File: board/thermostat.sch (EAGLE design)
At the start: 14 parts, among them IC1 7805TV, Q1 PSMN4R3-30PL

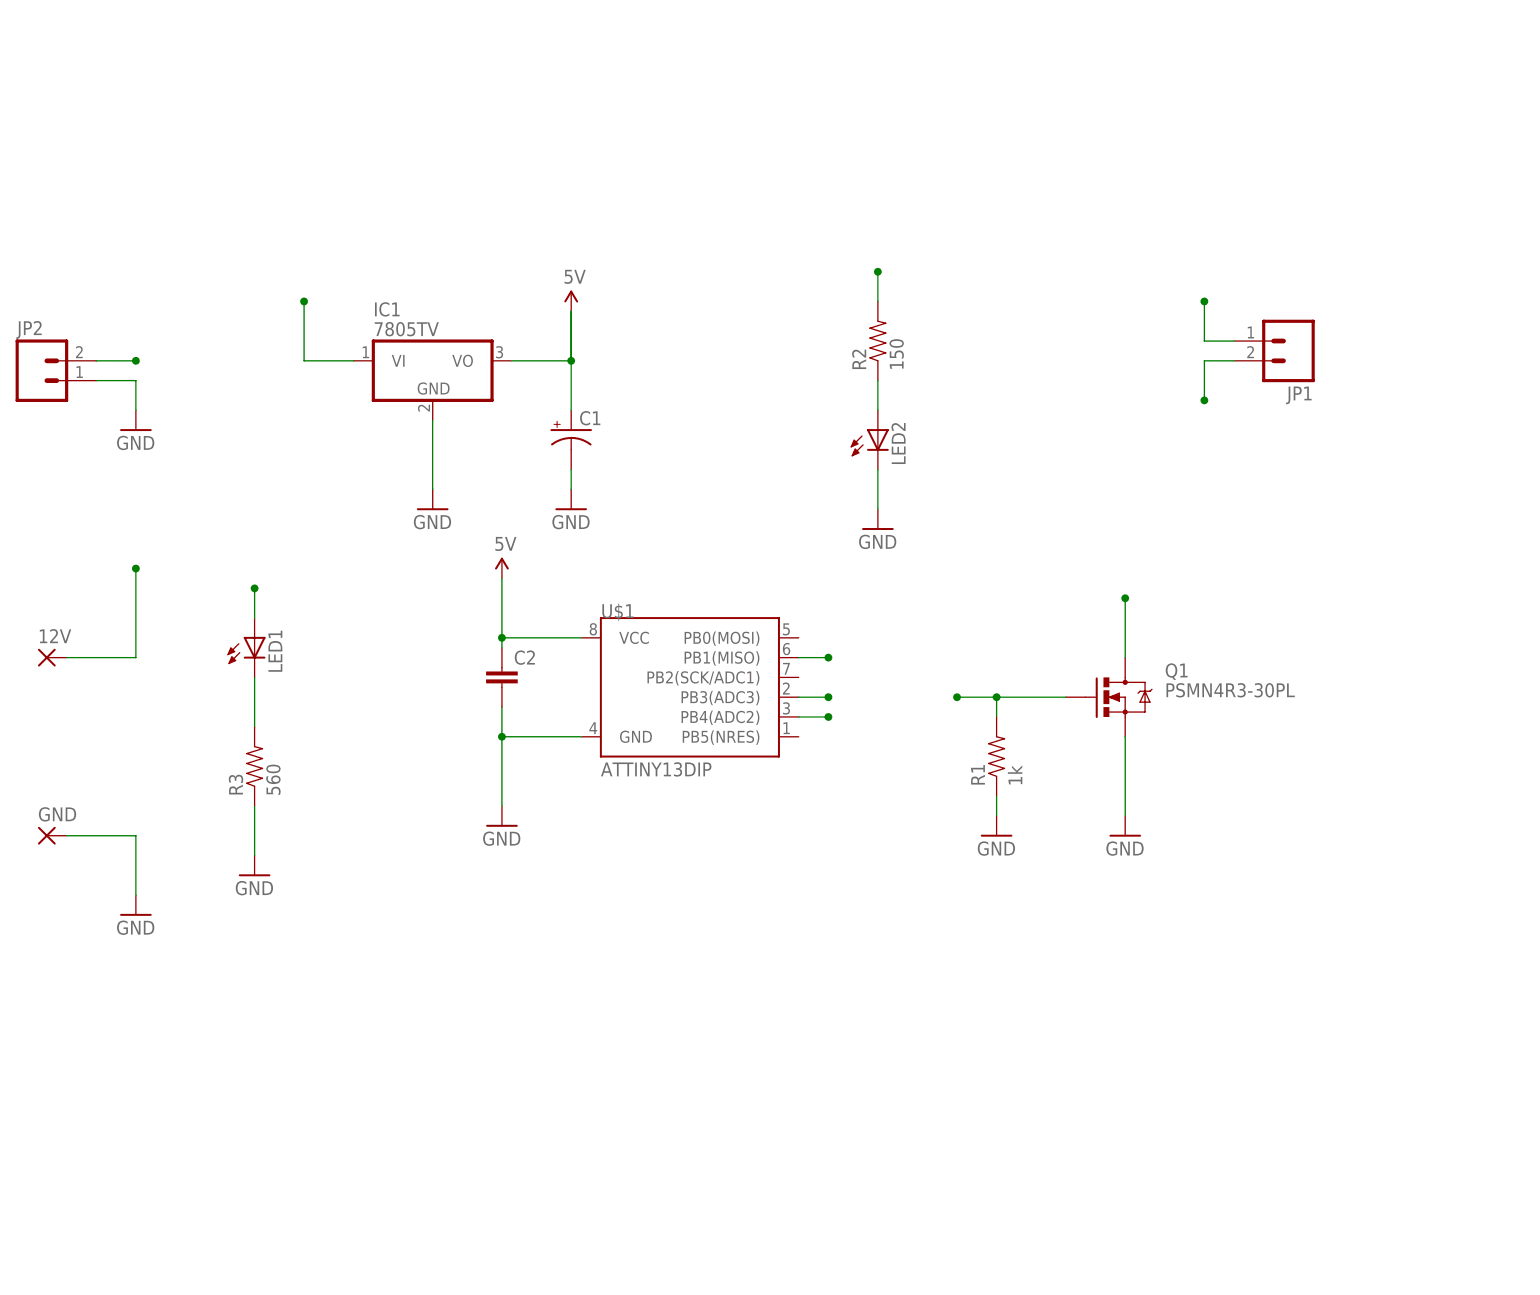
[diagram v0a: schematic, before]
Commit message: WIP: Protecting input and creating schematic
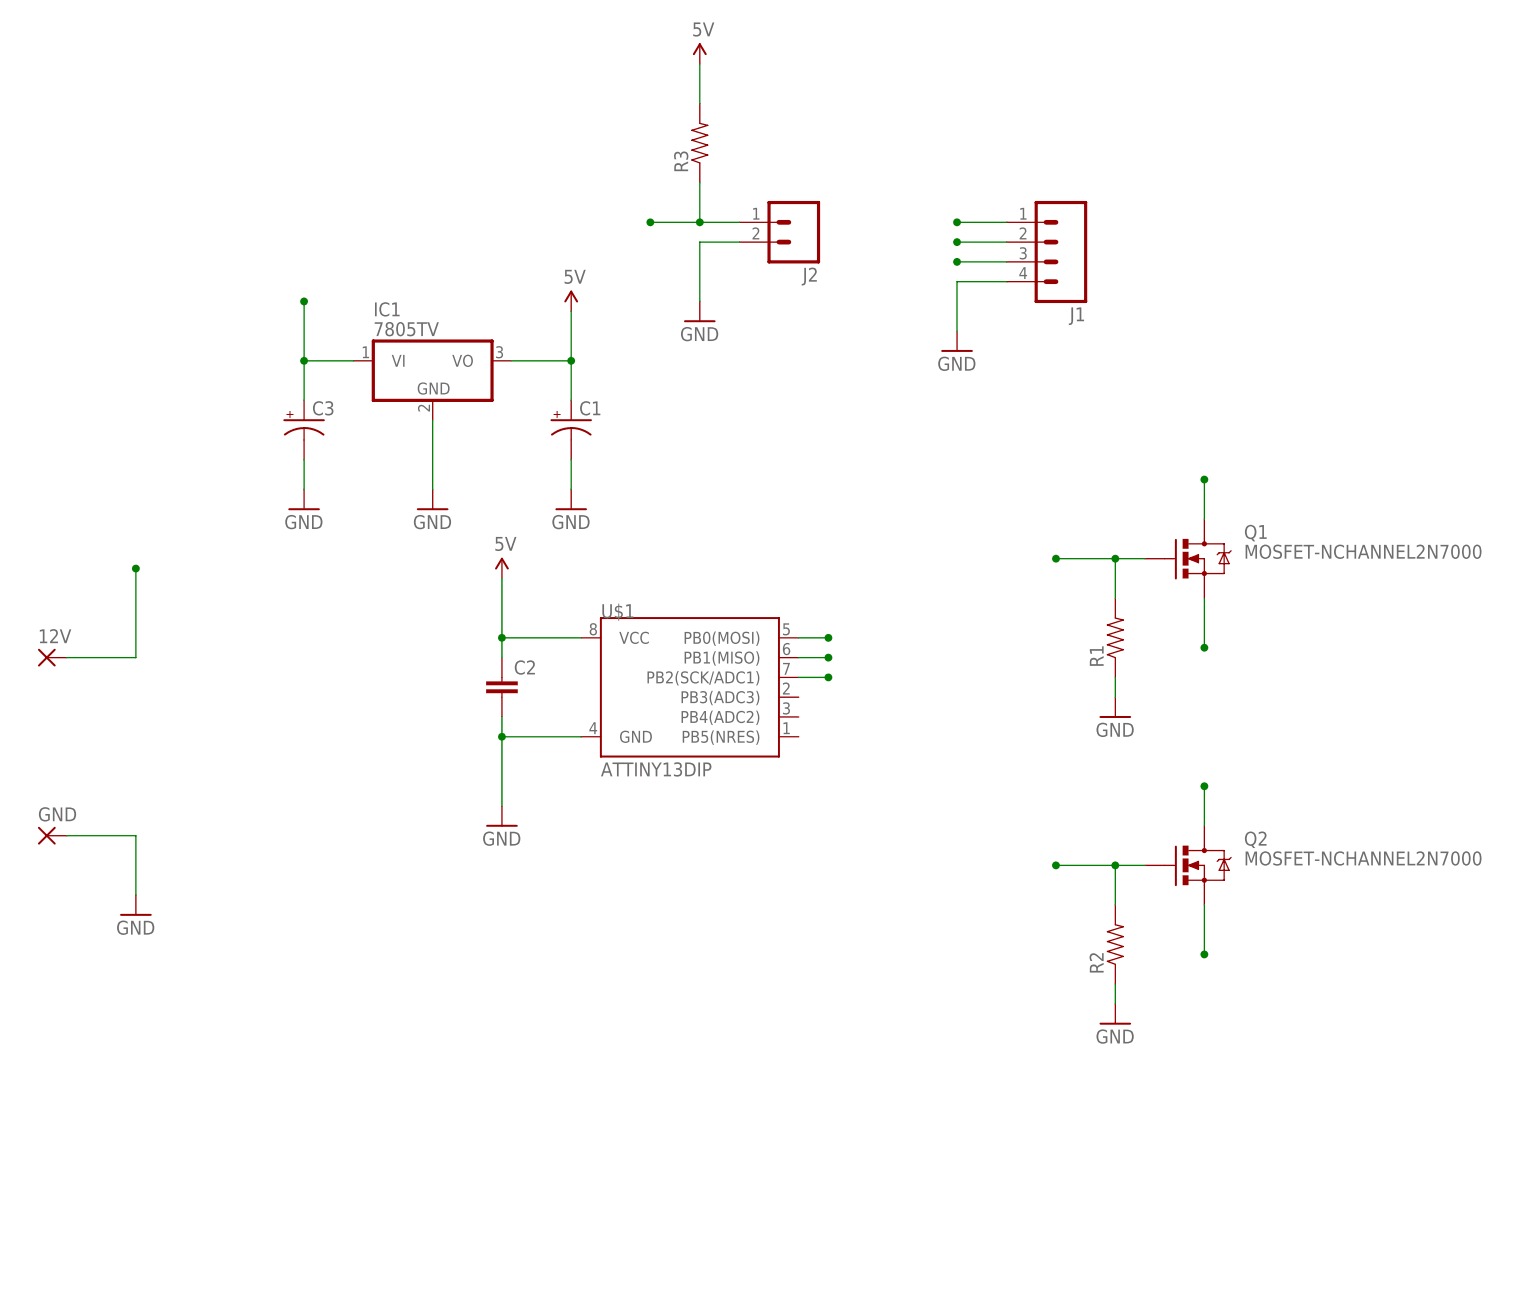
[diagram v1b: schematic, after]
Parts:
- removed JP1, JP2: M02SPRING-2.54-RA, SparkFun-Connectors:M02SPRING-2.54-RA
- removed LED1, LED2: (no value), SparkFun-LED:LED3MM
- added C3: (no value), SparkFun-Capacitors:CAP_POLPTH2
- added J1: (no value), SparkFun-Connectors:M04PTH
- added J2: (no value), SparkFun-Connectors:M02PTH
- added Q2: MOSFET-NCHANNEL2N7000, SparkFun-DiscreteSemi:MOSFET-NCHANNEL2N7000
- Q1: value PSMN4R3-30PL -> MOSFET-NCHANNEL2N7000; device SparkFun-DiscreteSemi:MOSFET-NCHANNELFQP30N06L -> SparkFun-DiscreteSemi:MOSFET-NCHANNEL2N7000
- R1: value 1k -> (none)
- R2: value 150 -> (none)
- R3: value 560 -> (none)
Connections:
- net PWM renamed HEAT_ON
- removed net DOOR_SW: JP2.2, U$1.PB3(ADC3)
- removed net LED_GND: JP1.1, Q1.D
- removed net N$1: LED1.C, R3.2
- removed net N$3: LED2.A, R2.1
- removed net STATUS_LED: R2.2, U$1.PB4(ADC2)
- new net HEAT_OFF: Q2.G, R2.2, U$1.PB0(MOSI)
- new net SWITCH_OFF: J1.1, Q2.S
- new net SWITCH_ON: J1.2, Q1.S
- new net SW_COMMON: J1.3, Q1.D, Q2.D
- new net THERMOSTAT_IN: J2.1, R3.1, U$1.PB2(SCK/ADC1)
- net 12V: now also C3.+; no longer JP1.2, LED1.A
- net 5V: now also R3.2
- net GND: now also C3.-, J1.4, J2.2, R2.1; no longer JP2.1, LED2.C, Q1.S, R3.1
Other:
- moved on the sheet: C1, C2, Q1, R1, R2, R3

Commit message: Board layout updates
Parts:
- removed R3: (no value), SparkFun-Passives:RESISTORAXIAL-0.3
- added Q3: MOSFET-NCHANNEL2N7000, SparkFun-DiscreteSemi:MOSFET-NCHANNEL2N7000
- added R4: 100k, SparkFun-Passives:RESISTORAXIAL-0.3
- added R5: 1k, SparkFun-Passives:RESISTORAXIAL-0.3
- C1: value (none) -> 10uF
- C2, C3: value (none) -> 0.1uF
- R1, R2: value (none) -> 100k
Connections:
- new net N$1: Q3.G, R4.1, R5.1
- new net SENSOR_IN: Q3.D, U$1.PB2(SCK/ADC1)
- net 5V: now also R4.2; no longer R3.2
- net GND: now also Q3.S
- net THERMOSTAT_IN: now also R5.2; no longer R3.1, U$1.PB2(SCK/ADC1)
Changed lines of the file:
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@@
 <part name="U$1" library="SparkFun-DigitalIC" deviceset="ATTINY13" device="DIP"/>
 <part name="IC1" library="linear" deviceset="78*" device="TV" technology="05"/>
-<part name="C1" library="SparkFun-Capacitors" deviceset="CAP_POL" device="PTH2"/>
-<part name="C2" library="SparkFun-Capacitors" deviceset="CAP" device="EZ"/>
+<part name="C1" library="SparkFun-Capacitors" deviceset="CAP_POL" device="PTH2" value="10uF"/>
+<part name="C2" library="SparkFun-Capacitors" deviceset="CAP" device="EZ" value="0.1uF"/>
 <part name="SUPPLY1" library="SparkFun-Aesthetics" deviceset="5V" device=""/>
 <part name="SUPPLY2" library="SparkFun-Aesthetics" deviceset="5V" device=""/>
@@
 <part name="GND" library="wirepad" deviceset="WIREPAD" device="2,54/0,8" value=""/>
 <part name="GND7" library="SparkFun-Aesthetics" deviceset="GND" device=""/>
-<part name="C3" library="SparkFun-Capacitors" deviceset="CAP_POL" device="PTH2"/>
+<part name="C3" library="SparkFun-Capacitors" deviceset="CAP_POL" device="PTH2" value="0.1uF"/>
 <part name="GND1" library="SparkFun-Aesthetics" deviceset="GND" device=""/>
 <part name="Q1" library="SparkFun-DiscreteSemi" deviceset="MOSFET-NCHANNEL" device="2N7000"/>
@@
 <part name="GND4" library="SparkFun-Aesthetics" deviceset="GND" device=""/>
 <part name="GND6" library="SparkFun-Aesthetics" deviceset="GND" device=""/>
-<part name="R1" library="SparkFun-Passives" deviceset="RESISTOR" device="AXIAL-0.3"/>
+<part name="R1" library="SparkFun-Passives" deviceset="RESISTOR" device="AXIAL-0.3" value="100k"/>
 <part name="GND8" library="SparkFun-Aesthetics" deviceset="GND" device=""/>
 <part name="Q2" library="SparkFun-DiscreteSemi" deviceset="MOSFET-NCHANNEL" device="2N7000"/>
-<part name="R2" library="SparkFun-Passives" deviceset="RESISTOR" device="AXIAL-0.3"/>
+<part name="R2" library="SparkFun-Passives" deviceset="RESISTOR" device="AXIAL-0.3" value="100k"/>
 <part name="GND9" library="SparkFun-Aesthetics" deviceset="GND" device=""/>
-<part name="R3" library="SparkFun-Passives" deviceset="RESISTOR" device="AXIAL-0.3"/>
-<part name="SUPPLY3" library="SparkFun-Aesthetics" deviceset="5V" device=""/>
+<part name="Q3" library="SparkFun-DiscreteSemi" deviceset="MOSFET-NCHANNEL" device="2N7000"/>
+<part name="GND10" library="SparkFun-Aesthetics" deviceset="GND" device=""/>
+<part name="R4" library="SparkFun-Passives" deviceset="RESISTOR" device="AXIAL-0.3" value="100k"/>
+<part name="SUPPLY4" library="SparkFun-Aesthetics" deviceset="5V" device=""/>
+<part name="R5" library="SparkFun-Passives" deviceset="RESISTOR" device="AXIAL-0.3" value="1k"/>
 </parts>
 <sheets>
@@
 <instance part="R2" gate="G$1" x="99.06" y="6.35" rot="R90"/>
 <instance part="GND9" gate="1" x="99.06" y="-3.81"/>
-<instance part="R3" gate="G$1" x="45.72" y="109.22" rot="R90"/>
-<instance part="SUPPLY3" gate="G$1" x="45.72" y="119.38"/>
+<instance part="Q3" gate="G$1" x="49.53" y="-22.86"/>
+<instance part="GND10" gate="1" x="49.53" y="-33.02"/>
+<instance part="R4" gate="G$1" x="34.29" y="-12.7" rot="R90"/>
+<instance part="SUPPLY4" gate="G$1" x="34.29" y="-2.54"/>
+<instance part="R5" gate="G$1" x="21.59" y="-22.86" rot="R180"/>
 </instances>
 <busses>
@@
 <pinref part="R2" gate="G$1" pin="1"/>
 </segment>
+<segment>
+<wire x1="49.53" y1="-27.94" x2="49.53" y2="-30.48" width="0.2032" layer="91"/>
+<pinref part="GND10" gate="1" pin="GND"/>
+<pinref part="Q3" gate="G$1" pin="S"/>
+</segment>
 </net>
 <net name="HEAT_ON" class="0">
@@
 </segment>
 <segment>
-<wire x1="45.72" y1="119.38" x2="45.72" y2="114.3" width="0.2032" layer="91"/>
-<pinref part="SUPPLY3" gate="G$1" pin="5V"/>
-<pinref part="R3" gate="G$1" pin="2"/>
+<pinref part="R4" gate="G$1" pin="2"/>
+<wire x1="34.29" y1="-7.62" x2="34.29" y2="-2.54" width="0.1524" layer="91"/>
+<pinref part="SUPPLY4" gate="G$1" pin="5V"/>
 </segment>
 </net>
@@
 <pinref part="J2" gate="G$1" pin="1"/>
 <wire x1="50.8" y1="99.06" x2="45.72" y2="99.06" width="0.1524" layer="91"/>
-<pinref part="R3" gate="G$1" pin="1"/>
-<wire x1="45.72" y1="104.14" x2="45.72" y2="99.06" width="0.1524" layer="91"/>
-<wire x1="45.72" y1="99.06" x2="39.37" y2="99.06" width="0.1524" layer="91"/>
 <junction x="45.72" y="99.06"/>
-<junction x="39.37" y="99.06"/>
-</segment>
-<segment>
-<pinref part="U$1" gate="G$1" pin="PB2(SCK/ADC1)"/>
-<wire x1="58.42" y1="40.64" x2="62.23" y2="40.64" width="0.1524" layer="91"/>
-<junction x="62.23" y="40.64"/>
+</segment>
+<segment>
+<pinref part="R5" gate="G$1" pin="2"/>
+<wire x1="16.51" y1="-22.86" x2="11.43" y2="-22.86" width="0.1524" layer="91"/>
+<junction x="11.43" y="-22.86"/>
 </segment>
 </net>
@@
 </segment>
 </net>
+<net name="N$1" class="0">
+<segment>
+<pinref part="Q3" gate="G$1" pin="G"/>
+<wire x1="41.91" y1="-22.86" x2="34.29" y2="-22.86" width="0.1524" layer="91"/>
+<wire x1="26.67" y1="-22.86" x2="34.29" y2="-22.86" width="0.1524" layer="91"/>
+<wire x1="34.29" y1="-22.86" x2="34.29" y2="-17.78" width="0.1524" layer="91"/>
+<junction x="34.29" y="-22.86"/>
+<pinref part="R4" gate="G$1" pin="1"/>
+<pinref part="R5" gate="G$1" pin="1"/>
+</segment>
+</net>
+<net name="SENSOR_IN" class="0">
+<segment>
+<pinref part="U$1" gate="G$1" pin="PB2(SCK/ADC1)"/>
+<wire x1="58.42" y1="40.64" x2="62.23" y2="40.64" width="0.1524" layer="91"/>
+<junction x="62.23" y="40.64"/>
+</segment>
+<segment>
+<pinref part="Q3" gate="G$1" pin="D"/>
+<wire x1="49.53" y1="-17.78" x2="49.53" y2="-10.16" width="0.1524" layer="91"/>
+<junction x="49.53" y="-10.16"/>
+</segment>
+</net>

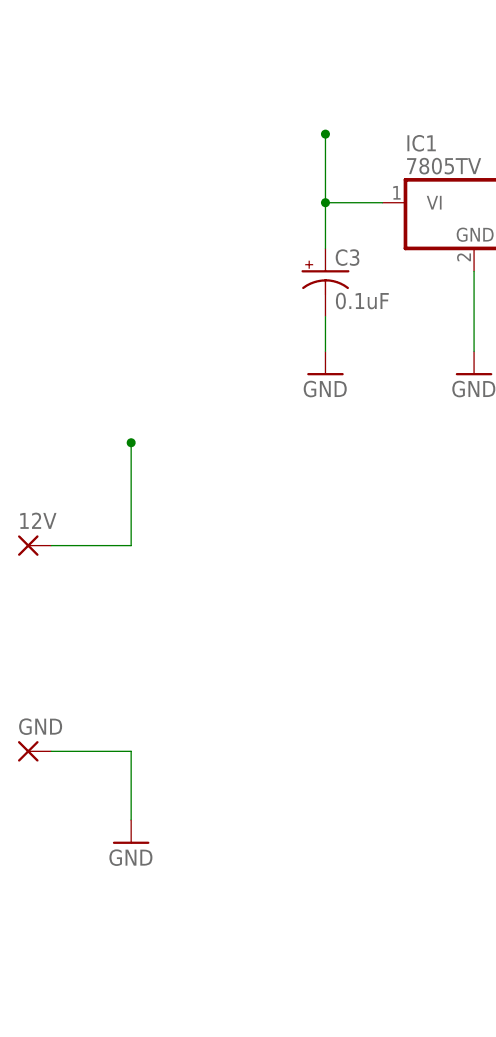
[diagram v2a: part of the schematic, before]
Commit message: Production build & source
The Thermostat relay board is successfully working in the spare bedroom.
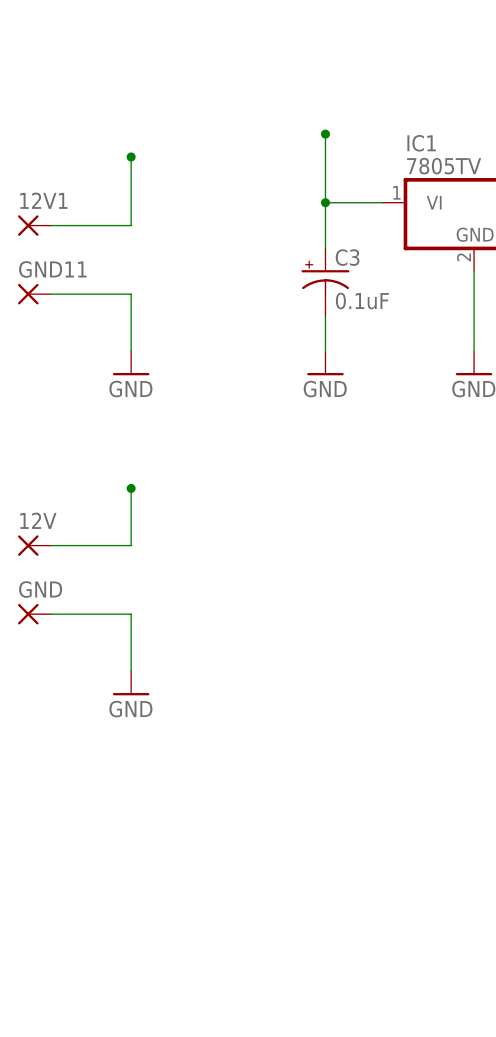
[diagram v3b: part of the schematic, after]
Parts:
- added 12V1, GND11: WIREPAD2,54/0,8, wirepad:WIREPAD2,54/0,8
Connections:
- net 12V: now also 12V1.P
- net GND: now also GND11.P
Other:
- moved on the sheet: GND
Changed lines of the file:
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@@
 <?xml version="1.0" encoding="utf-8"?>
 <!DOCTYPE eagle SYSTEM "eagle.dtd">
-<eagle version="8.0.0">
+<eagle version="7.7.0">
 <drawing>
 <settings>
@@
 <part name="SUPPLY4" library="SparkFun-Aesthetics" deviceset="5V" device=""/>
 <part name="R5" library="SparkFun-Passives" deviceset="RESISTOR" device="AXIAL-0.3" value="1k"/>
+<part name="GND12" library="SparkFun-Aesthetics" deviceset="GND" device=""/>
+<part name="GND11" library="wirepad" deviceset="WIREPAD" device="2,54/0,8" value=""/>
+<part name="12V1" library="wirepad" deviceset="WIREPAD" device="2,54/0,8" value=""/>
 </parts>
 <sheets>
@@
 <instance part="GND5" gate="1" x="29.21" y="62.23"/>
 <instance part="12V" gate="G$1" x="-38.1" y="43.18"/>
-<instance part="GND" gate="G$1" x="-38.1" y="20.32"/>
-<instance part="GND7" gate="1" x="-26.67" y="10.16"/>
+<instance part="GND" gate="G$1" x="-38.1" y="35.56"/>
+<instance part="GND7" gate="1" x="-26.67" y="26.67"/>
 <instance part="C3" gate="G$1" x="-5.08" y="73.66"/>
 <instance part="GND1" gate="1" x="-5.08" y="62.23"/>
@@
 <instance part="SUPPLY4" gate="G$1" x="34.29" y="-2.54"/>
 <instance part="R5" gate="G$1" x="21.59" y="-22.86" rot="R180"/>
+<instance part="GND12" gate="1" x="-26.67" y="62.23"/>
+<instance part="GND11" gate="G$1" x="-38.1" y="71.12"/>
+<instance part="12V1" gate="G$1" x="-38.1" y="78.74"/>
 </instances>
 <busses>
@@
 <segment>
 <pinref part="GND" gate="G$1" pin="P"/>
-<wire x1="-35.56" y1="20.32" x2="-26.67" y2="20.32" width="0.2032" layer="91"/>
-<wire x1="-26.67" y1="20.32" x2="-26.67" y2="12.7" width="0.2032" layer="91"/>
+<wire x1="-35.56" y1="35.56" x2="-26.67" y2="35.56" width="0.2032" layer="91"/>
+<wire x1="-26.67" y1="35.56" x2="-26.67" y2="29.21" width="0.2032" layer="91"/>
 <pinref part="GND7" gate="1" pin="GND"/>
 </segment>
@@
 <pinref part="GND10" gate="1" pin="GND"/>
 <pinref part="Q3" gate="G$1" pin="S"/>
+</segment>
+<segment>
+<wire x1="-35.56" y1="71.12" x2="-26.67" y2="71.12" width="0.2032" layer="91"/>
+<pinref part="GND11" gate="G$1" pin="P"/>
+</segment>
+<segment>
+<wire x1="-26.67" y1="71.12" x2="-26.67" y2="64.77" width="0.2032" layer="91"/>
+<pinref part="GND12" gate="1" pin="GND"/>
 </segment>
 </net>
@@
 <pinref part="12V" gate="G$1" pin="P"/>
 <wire x1="-35.56" y1="43.18" x2="-26.67" y2="43.18" width="0.2032" layer="91"/>
-<wire x1="-26.67" y1="43.18" x2="-26.67" y2="54.61" width="0.2032" layer="91"/>
-<junction x="-26.67" y="54.61"/>
+<wire x1="-26.67" y1="43.18" x2="-26.67" y2="49.53" width="0.2032" layer="91"/>
+<junction x="-26.67" y="49.53"/>
+</segment>
+<segment>
+<wire x1="-35.56" y1="78.74" x2="-26.67" y2="78.74" width="0.1524" layer="91"/>
+<wire x1="-26.67" y1="78.74" x2="-26.67" y2="86.36" width="0.1524" layer="91"/>
+<junction x="-26.67" y="86.36"/>
+<pinref part="12V1" gate="G$1" pin="P"/>
 </segment>
 </net>
